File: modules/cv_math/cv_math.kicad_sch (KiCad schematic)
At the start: 8 parts

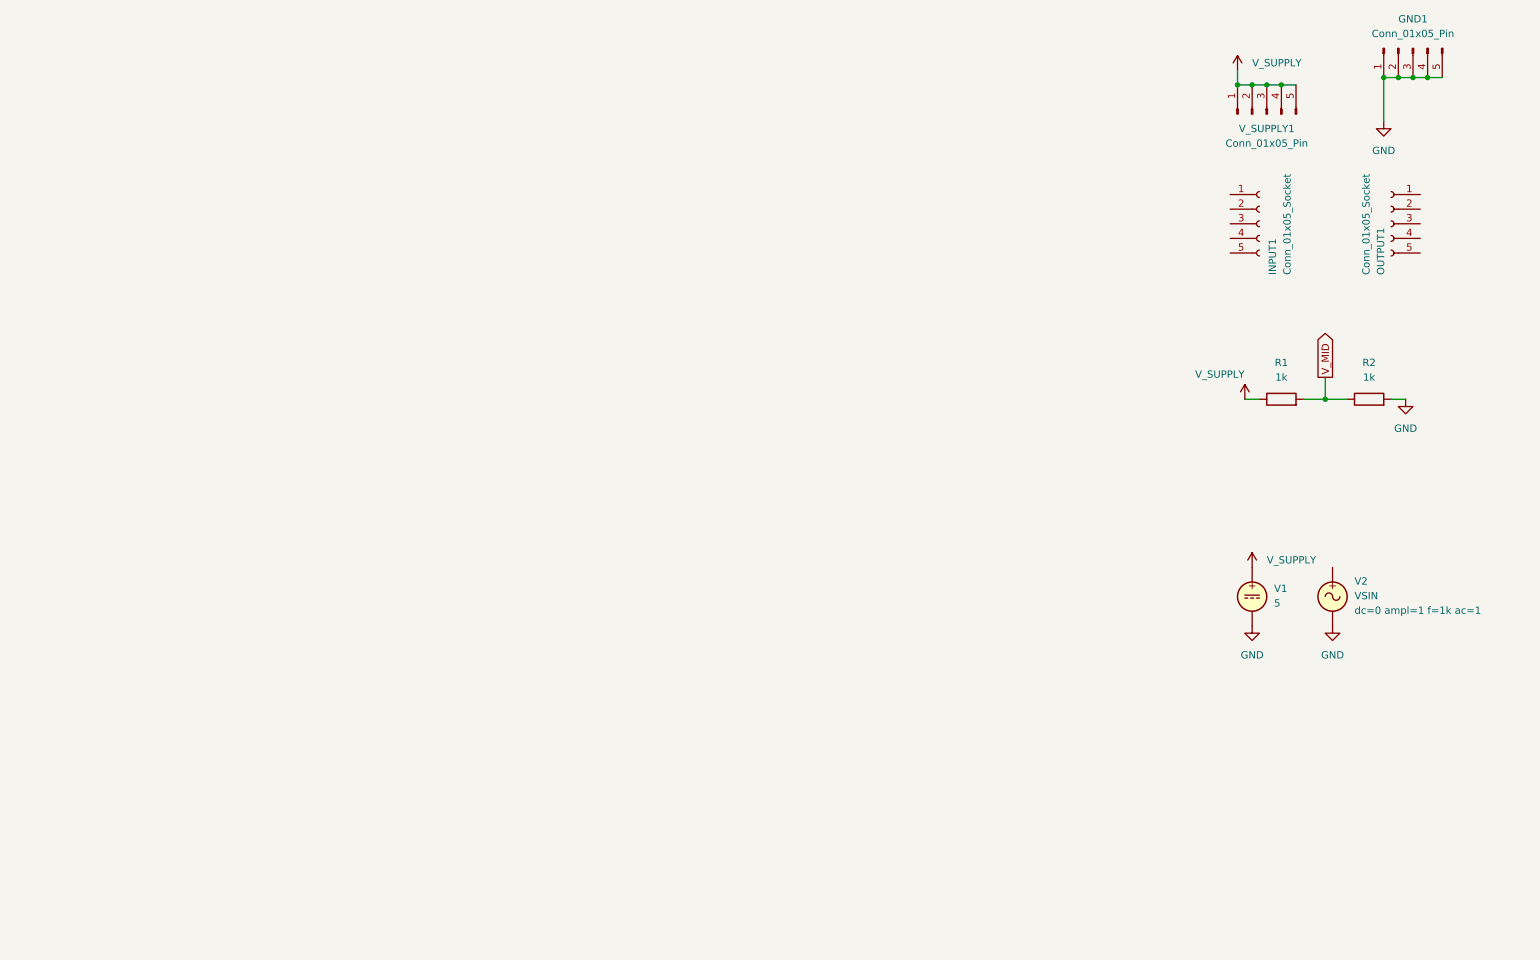
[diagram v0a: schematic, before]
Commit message: Implement the schematic of cv_math
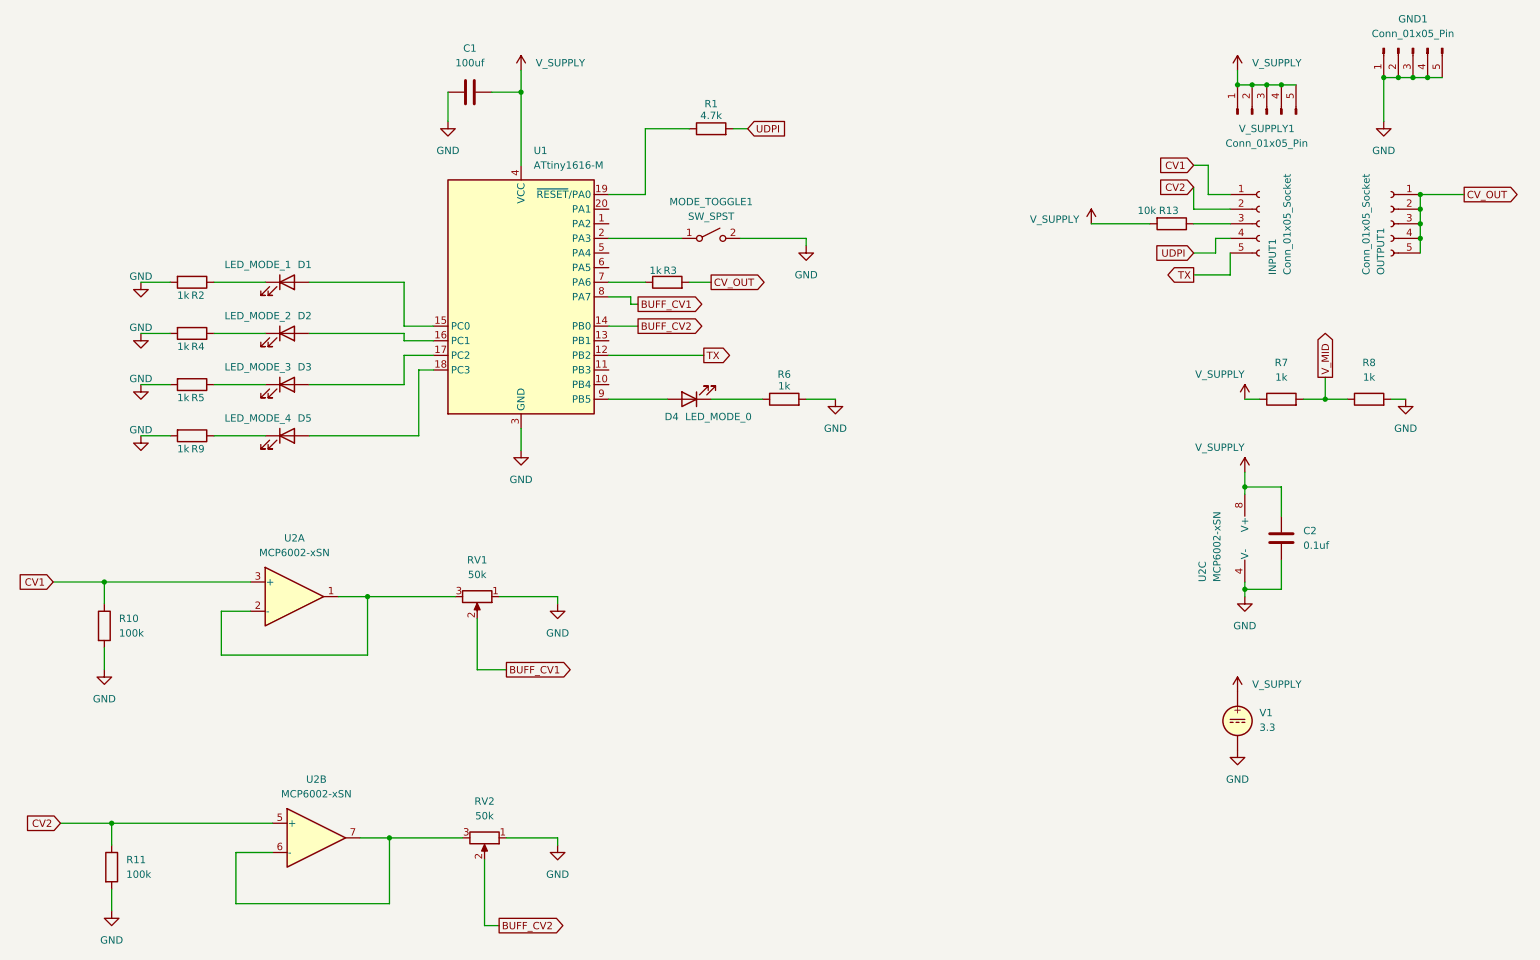
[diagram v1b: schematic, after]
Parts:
- removed V2: VSIN, symbol Simulation_SPICE:VSIN
- added C1: 100uf, Capacitor_SMD:C_1206_3216Metric, symbol Device:C
- added C2: 0.1uf, Capacitor_SMD:C_0402_1005Metric, symbol Device:C
- added D1: LED_MODE_1, LED_SMD:LED_0603_1608Metric, symbol Device:LED
- added D2: LED_MODE_2, LED_SMD:LED_0603_1608Metric, symbol Device:LED
- added D3: LED_MODE_3, LED_SMD:LED_0603_1608Metric, symbol Device:LED
- added D4: LED_MODE_0, LED_SMD:LED_0603_1608Metric, symbol Device:LED
- added D5: LED_MODE_4, LED_SMD:LED_0603_1608Metric, symbol Device:LED
- added MODE_TOGGLE1: SW_SPST, BreadModular_MISC:SPST_TS-1187A-B-A-B, symbol Switch:SW_SPST
- added R1: 4.7k, Resistor_SMD:R_0402_1005Metric, symbol Device:R
- added R10, R11: 100k, Resistor_SMD:R_0402_1005Metric, symbol Device:R
- added R13: 10k, Resistor_SMD:R_0402_1005Metric, symbol Device:R
- added R2, R3, R4, R5, R6, R9: 1k, Resistor_SMD:R_0402_1005Metric, symbol Device:R
- added RV1, RV2: 50k, BreadModular_Pots:Potentiometer_RV09, symbol Device:R_Potentiometer
- added U1: ATtiny1616-M, Package_DFN_QFN:VQFN-20-1EP_3x3mm_P0.4mm_EP1.7x1.7mm, symbol MCU_Microchip_ATtiny:ATtiny1616-M
- added U2: MCP6002-xSN, Package_SO:SOIC-8-1EP_3.9x4.9mm_P1.27mm_EP2.29x3mm, symbol Amplifier_Operational:MCP6002-xSN
- R7: renamed from R1; footprint (none) -> Resistor_SMD:R_0402_1005Metric
- R8: renamed from R2; footprint (none) -> Resistor_SMD:R_0402_1005Metric
- V1: value 5 -> 3.3
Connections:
- net GND: now also C1.1, C2.2, MODE_TOGGLE1.2 (B), R10.2, R11.2, R2.2, R4.2, R5.2, R6.2, R9.2, RV1.1, RV2.1, U1.21 (GND), U1.3 (GND), U2.4 (V-)
- net V_SUPPLY: now also C1.2, C2.1, R13.2, U1.4 (VCC), U2.8 (V+)
- net CV_OUT: now reaches OUTPUT1.1 (Pin_1)
- net CV_OUT: now also OUTPUT1.2 (Pin_2), OUTPUT1.3 (Pin_3), OUTPUT1.4 (Pin_4), OUTPUT1.5 (Pin_5), R3.2
- net CV1: now reaches INPUT1.1 (Pin_1)
- net CV1: now also R10.1, U2.3 (+)
- net CV2: now reaches INPUT1.2 (Pin_2)
- net CV2: now also R11.1, U2.5 (+)
- net at INPUT1.3 (Pin_3): now also R13.1
- net UDPI: now reaches INPUT1.4 (Pin_4)
- net UDPI: now also R1.2
- net TX: now reaches INPUT1.5 (Pin_5)
- net TX: now also U1.12 (PB2)
- new net: D5.1 (K), R9.1
- new net: D5.2 (A), U1.18 (PC3)
- new net: RV1.3, U2.1, U2.2 (-)
- new net: R3.1, U1.7 (PA6)
- new net: D1.1 (K), R2.1
- new net: D1.2 (A), U1.15 (PC0)
- new net: D3.1 (K), R5.1
- new net: D3.2 (A), U1.17 (PC2)
- new net: D4.1 (K), R6.1
- new net: D4.2 (A), U1.9 (PB5)
- new net: R1.1, U1.19 (~{RESET}/PA0)
- new net: D2.2 (A), U1.16 (PC1)
- new net: MODE_TOGGLE1.1 (A), U1.2 (PA3)
- new net: D2.1 (K), R4.1
- new net: RV2.3, U2.6 (-), U2.7
- new net BUFF_CV1: RV1.2, U1.8 (PA7)
- new net BUFF_CV2: RV2.2, U1.14 (PB0)
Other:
- moved on the sheet: V1

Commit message: Finished cv_math PCB routing
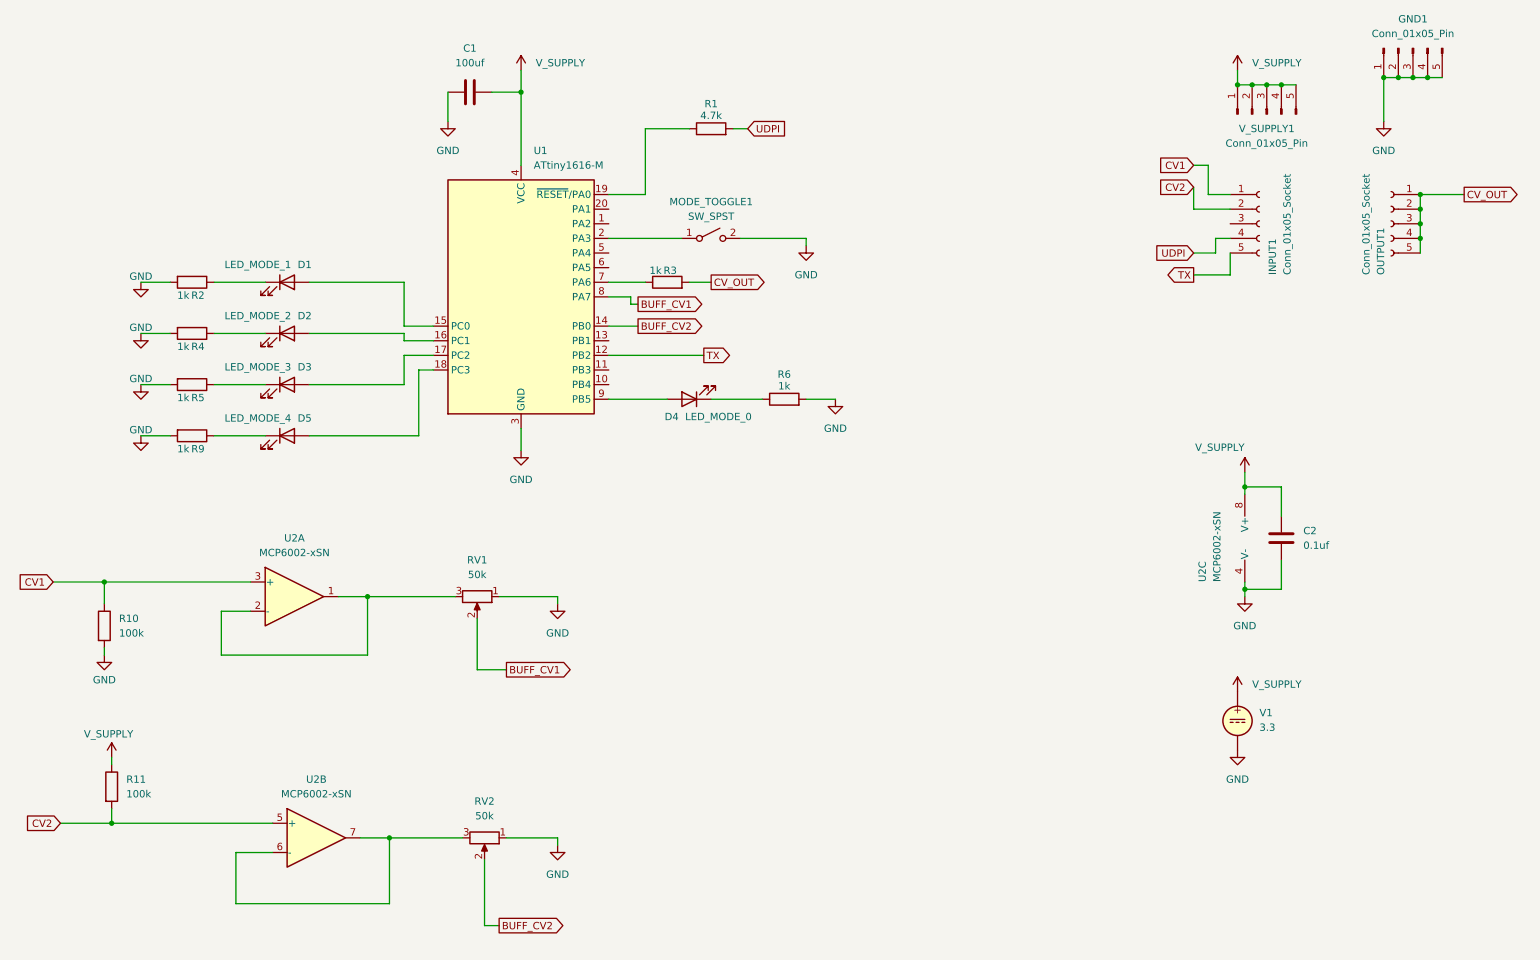
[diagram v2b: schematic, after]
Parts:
- removed R13: 10k, Resistor_SMD:R_0402_1005Metric, symbol Device:R
- removed R7, R8: 1k, Resistor_SMD:R_0402_1005Metric, symbol Device:R
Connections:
- net CV2: now also R11.2; no longer R11.1
- net GND: no longer R11.2
- net V_SUPPLY: now also R11.1
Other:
- moved on the sheet: R11
